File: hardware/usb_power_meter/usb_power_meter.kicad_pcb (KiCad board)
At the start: 4 copper layers, 37 x 39 mm, 39 parts, among them J1 KH-1.27PH180-2X5P-L7.2-SMT, J2 917-P81A202ES60201, J4 A/F LCPTrue color1.2pillar_C4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, Q1 2N7002, Q2 IRML6401, U1 nRF52833-QDxx, U2 INA226, X1 32Mhz crystal, X2 32.768kHz crystal

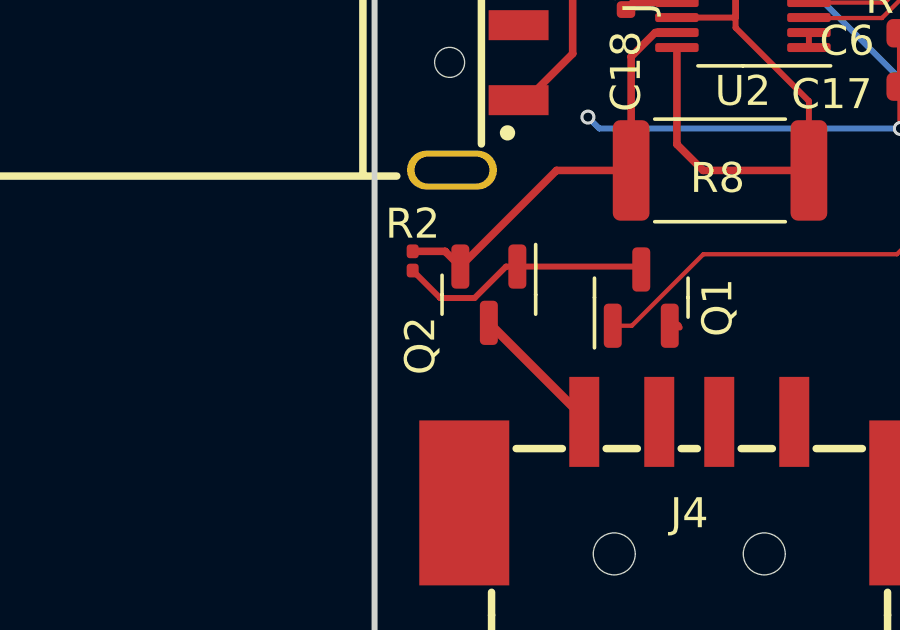
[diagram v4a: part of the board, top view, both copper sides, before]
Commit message: Add a protection diode
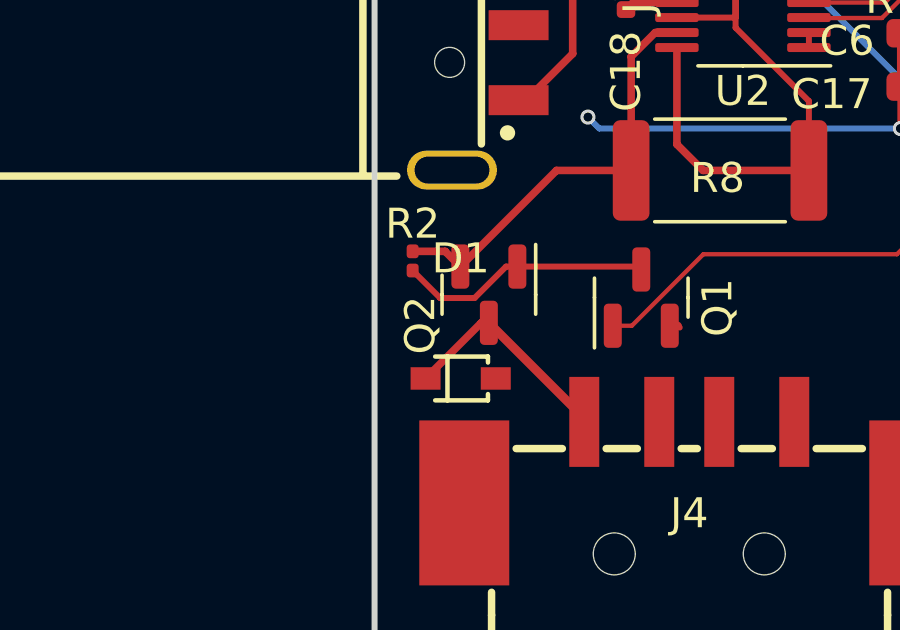
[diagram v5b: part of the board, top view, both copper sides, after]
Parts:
- added D1: 1N5819WS, easyeda2kicad:SOD-323_L1.8-W1.3-LS2.5-RD, F.Cu at (102.9, 83.8)
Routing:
- net Net-(D1-C): track 4.62 -> 7.50 mm
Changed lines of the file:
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@@
   (net 40 "unconnected-(J4-D+-Pad2)")
   (net 41 "unconnected-(J4-D--Pad3)")
-  (net 42 "Net-(J4-VCC)")
+  (net 42 "Net-(D1-C)")
   (net 43 "unconnected-(J4-Pad5)")
   (net 44 "unconnected-(J4-Pad6)")
@@
     (property "ki_keywords" "transistor PMOS P-MOS P-MOSFET")
     (attr smd)
-    (fp_text reference "Q2" (at 1.6995 2.286 90) (layer "F.SilkS")
+    (fp_text reference "Q2" (at 1.0135 2.286 90) (layer "F.SilkS")
         (effects (font (size 1 1) (thickness 0.15)))
     )
@@
       (net 34 "Net-(Q2-S)") (pinfunction "S") (pintype "passive"))
     (pad "3" smd roundrect (at 0.9375 0 270) (size 1.475 0.6) (layers "F.Cu" "F.Paste" "F.Mask") (roundrect_rratio 0.25)
-      (net 42 "Net-(J4-VCC)") (pinfunction "D") (pintype "passive"))
+      (net 42 "Net-(D1-C)") (pinfunction "D") (pintype "passive"))
     (model "${KICAD6_3DMODEL_DIR}/Package_TO_SOT_SMD.3dshapes/SOT-23.wrl"
       (offset (xyz 0 0 0))
@@
       (scale (xyz 1 1 1))
       (rotate (xyz 0 0 0))
+    )
+  )
+  (footprint "easyeda2kicad:SOD-323_L1.8-W1.3-LS2.5-RD" (layer "F.Cu")
+    (at 102.87 83.82)
+    (property "JLC Part" "Basic Part")
+    (property "LCSC Part" "C191023")
+    (property "Manufacturer" "Hottech(合科泰)")
+    (property "Sheetfile" "usb_power_meter.kicad_sch")
+    (property "Sheetname" "")
+    (attr smd)
+    (fp_text reference "D1" (at 0 -4) (layer "F.SilkS")
+        (effects (font (size 1 1) (thickness 0.15)))
+    )
+    (fp_text value "1N5819WS" (at 0 4) (layer "F.Fab")
+        (effects (font (size 1 1) (thickness 0.15)))
+    )
+    (fp_text user "${REFERENCE}" (at 0 0) (layer "F.Fab")
+        (effects (font (size 1 1) (thickness 0.15)))
+    )
+    (fp_line (start -0.85 -0.73) (end 0.91 -0.73)
+      (stroke (width 0.15) (type solid)) (layer "F.SilkS"))
+    (fp_line (start -0.85 0.73) (end 0.91 0.73)
+      (stroke (width 0.15) (type solid)) (layer "F.SilkS"))
+    (fp_line (start -0.44 -0.73) (end -0.44 0.73)
+      (stroke (width 0.15) (type solid)) (layer "F.SilkS"))
+    (fp_line (start 0.91 -0.73) (end 0.91 -0.53)
+      (stroke (width 0.15) (type solid)) (layer "F.SilkS"))
+    (fp_line (start 0.91 0.73) (end 0.91 0.52)
+      (stroke (width 0.15) (type solid)) (layer "F.SilkS"))
+    (fp_circle (center -1.22 0.65) (end -1.19 0.65)
+      (stroke (width 0.06) (type solid)) (fill none) (layer "F.Fab"))
+    (pad "1" smd rect (at -1.17 0) (size 1 0.75) (layers "F.Cu" "F.Paste" "F.Mask")
+      (net 42 "Net-(D1-C)") (pinfunction "C") (pintype "unspecified"))
+    (pad "2" smd rect (at 1.17 0) (size 1 0.75) (layers "F.Cu" "F.Paste" "F.Mask")
+      (net 1 "GND") (pinfunction "A") (pintype "unspecified"))
+    (model "${EASYEDA2KICAD}/easyeda2kicad.3dshapes/SOD-323_L1.7-W1.3-H1.1-LS2.5.wrl"
+      (offset (xyz -0.14 0 -0))
+      (scale (xyz 1 1 1))
+      (rotate (xyz 0 0 180))
     )
   )
@@
       (net 41 "unconnected-(J4-D--Pad3)") (pinfunction "D-") (pintype "unspecified+no_connect"))
     (pad "4" smd rect (at -3.5 -1.35) (size 1 3) (layers "F.Cu" "F.Paste" "F.Mask")
-      (net 42 "Net-(J4-VCC)") (pinfunction "VCC") (pintype "unspecified"))
+      (net 42 "Net-(D1-C)") (pinfunction "VCC") (pintype "unspecified"))
     (pad "5" smd rect (at -7.5 1.35 90) (size 5.5 3) (layers "F.Cu" "F.Paste" "F.Mask")
       (net 43 "unconnected-(J4-Pad5)") (pinfunction "5") (pintype "unspecified+no_connect"))
@@
   (segment (start 106.99 85.268) (end 106.99 85.146) (width 0.3) (layer "F.Cu") (net 42))
   (segment (start 106.99 85.146) (end 103.81 81.966) (width 0.3) (layer "F.Cu") (net 42))
+  (segment (start 101.7 83.82) (end 103.554 81.966) (width 0.254) (layer "F.Cu") (net 42))
+  (segment (start 103.554 81.966) (end 103.81 81.966) (width 0.254) (layer "F.Cu") (net 42))
   (segment (start 125.274 74.22) (end 125.274 73.6555) (width 0.2) (layer "F.Cu") (net 45))
   (segment (start 126.67 87.345) (end 126.67 94.158) (width 0.2) (layer "F.Cu") (net 45))

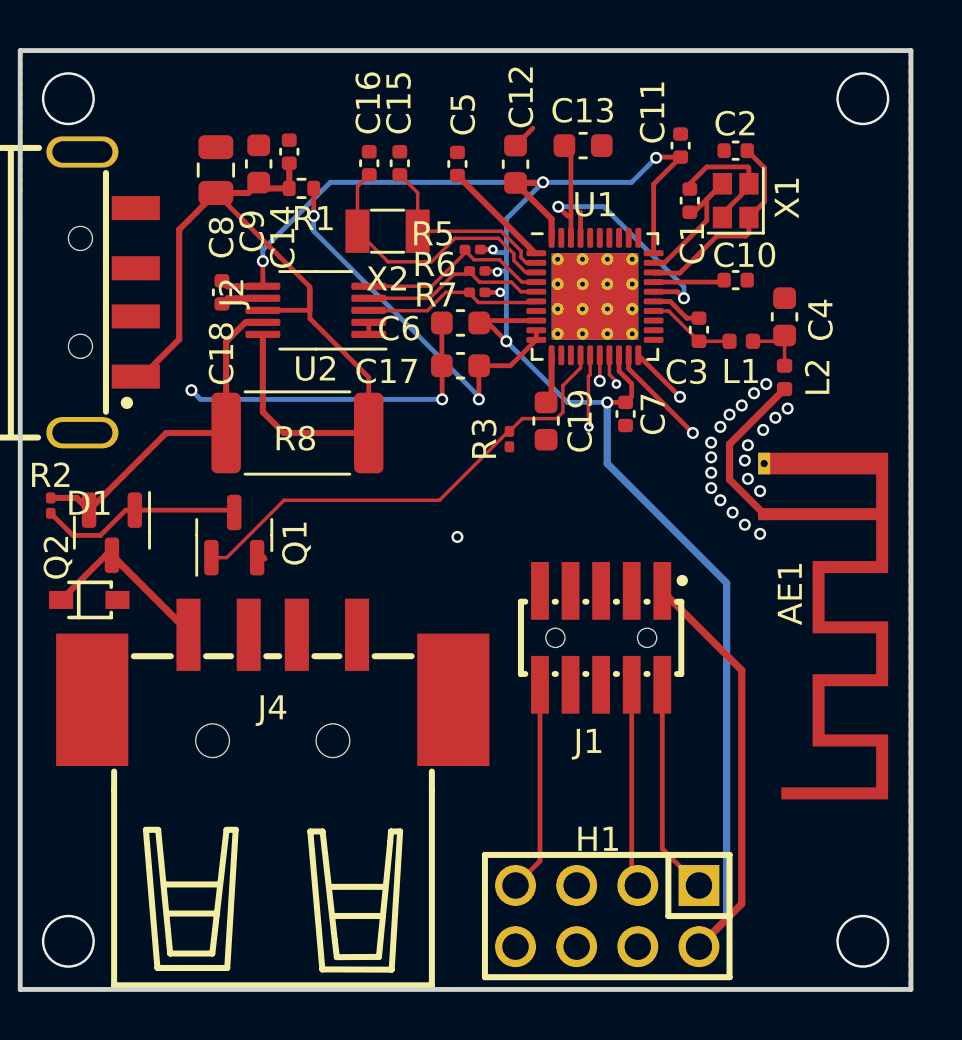
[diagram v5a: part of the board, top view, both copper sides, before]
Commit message: Add stitching vias
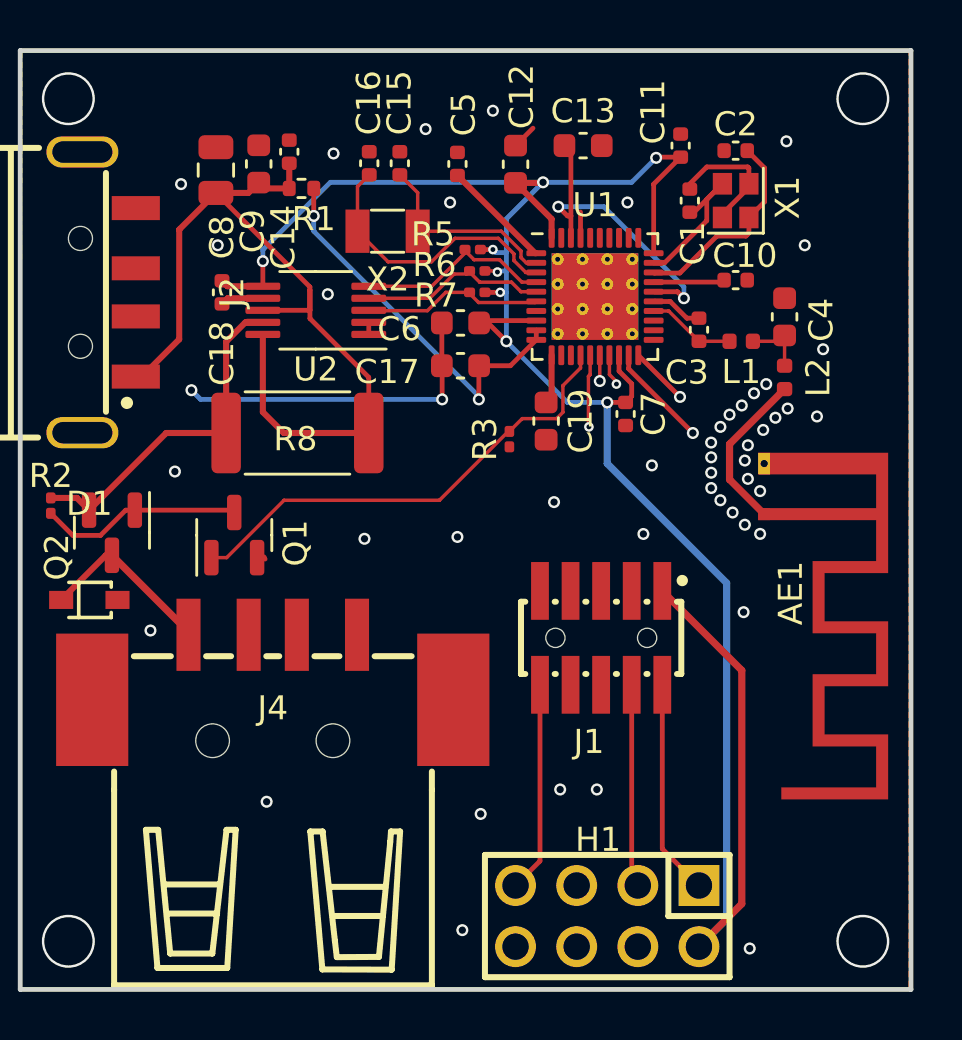
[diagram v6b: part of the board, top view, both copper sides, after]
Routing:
- net GND: vias 26 -> 51
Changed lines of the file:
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@@
   (segment (start 130.218 65.834) (end 128.518 65.834) (width 0.2) (layer "F.Cu") (net 1))
   (segment (start 123.274 68.7805) (end 123.274 67.709) (width 0.2) (layer "F.Cu") (net 1))
+  (via (at 126.238 78.232) (size 0.5) (drill 0.3) (layers "F.Cu" "B.Cu") (free) (net 1))
   (via (at 130.099 80.696) (size 0.5) (drill 0.3) (layers "F.Cu" "B.Cu") (free) (net 1))
   (via (at 118.161 81.204) (size 0.5) (drill 0.3) (layers "F.Cu" "B.Cu") (free) (net 1))
+  (via (at 130.048 84.328) (size 0.5) (drill 0.3) (layers "F.Cu" "B.Cu") (free) (net 1))
+  (via (at 106.426 78.486) (size 0.5) (drill 0.3) (layers "F.Cu" "B.Cu") (free) (net 1))
   (via (at 135 63) (size 2.2) (drill 2) (layers "F.Cu" "B.Cu") (net 1))
+  (via (at 117.856 67.31) (size 0.5) (drill 0.3) (layers "F.Cu" "B.Cu") (free) (net 1))
   (via (at 130.226 77.394) (size 0.5) (drill 0.3) (layers "F.Cu" "B.Cu") (free) (net 1))
   (via (at 130.734 81.077) (size 0.5) (drill 0.3) (layers "F.Cu" "B.Cu") (free) (net 1))
+  (via (at 125.884034 81.080088) (size 0.5) (drill 0.3) (layers "F.Cu" "B.Cu") (free) (net 1))
+  (via (at 119.126 92.71) (size 0.5) (drill 0.3) (layers "F.Cu" "B.Cu") (free) (net 1))
+  (via (at 133.35 73.406) (size 0.5) (drill 0.3) (layers "F.Cu" "B.Cu") (free) (net 1))
   (via (at 130.988 74.854) (size 0.5) (drill 0.3) (layers "F.Cu" "B.Cu") (free) (net 1))
   (via (at 128.698591 77.283465) (size 0.5) (drill 0.3) (layers "F.Cu" "B.Cu") (free) (net 1))
   (via (at 117.526 75.489) (size 0.5) (drill 0.3) (layers "F.Cu" "B.Cu") (free) (net 1))
   (via (at 102 98) (size 2.2) (drill 2) (layers "F.Cu" "B.Cu") (free) (net 1))
+  (via (at 133.096 76.2) (size 0.5) (drill 0.3) (layers "F.Cu" "B.Cu") (free) (net 1))
+  (via (at 114.3 81.28) (size 0.5) (drill 0.3) (layers "F.Cu" "B.Cu") (free) (net 1))
   (via (at 130.226 78.791) (size 0.5) (drill 0.3) (layers "F.Cu" "B.Cu") (free) (net 1))
+  (via (at 130.302 98.298) (size 0.5) (drill 0.3) (layers "F.Cu" "B.Cu") (free) (net 1))
+  (via (at 131.826 64.77) (size 0.5) (drill 0.3) (layers "F.Cu" "B.Cu") (free) (net 1))
   (via (at 128.701465 77.895732) (size 0.5) (drill 0.3) (layers "F.Cu" "B.Cu") (free) (net 1))
+  (via (at 118.364 97.536) (size 0.5) (drill 0.3) (layers "F.Cu" "B.Cu") (free) (net 1))
   (via (at 130.861 76.759) (size 0.5) (drill 0.3) (layers "F.Cu" "B.Cu") (free) (net 1))
   (via (at 128.702 78.537) (size 0.5) (drill 0.3) (layers "F.Cu" "B.Cu") (free) (net 1))
@@
   (via (at 131.369 76.251) (size 0.5) (drill 0.3) (layers "F.Cu" "B.Cu") (free) (net 1))
   (via (at 128.702 79.172) (size 0.5) (drill 0.3) (layers "F.Cu" "B.Cu") (free) (net 1))
+  (via (at 132.588 69.088) (size 0.5) (drill 0.3) (layers "F.Cu" "B.Cu") (free) (net 1))
+  (via (at 123.952 91.694) (size 0.5) (drill 0.3) (layers "F.Cu" "B.Cu") (free) (net 1))
+  (via (at 113.01509 65.275609) (size 0.5) (drill 0.3) (layers "F.Cu" "B.Cu") (free) (net 1))
+  (via (at 116.84 64.262) (size 0.5) (drill 0.3) (layers "F.Cu" "B.Cu") (free) (net 1))
   (via (at 129.464 76.124) (size 0.5) (drill 0.3) (layers "F.Cu" "B.Cu") (free) (net 1))
   (via (at 130.734 79.299) (size 0.5) (drill 0.3) (layers "F.Cu" "B.Cu") (free) (net 1))
+  (via (at 110.236 92.202) (size 0.5) (drill 0.3) (layers "F.Cu" "B.Cu") (free) (net 1))
   (via (at 129.083 76.632) (size 0.5) (drill 0.3) (layers "F.Cu" "B.Cu") (free) (net 1))
+  (via (at 122.428 91.694) (size 0.5) (drill 0.3) (layers "F.Cu" "B.Cu") (free) (net 1))
+  (via (at 106.68 66.548) (size 0.5) (drill 0.3) (layers "F.Cu" "B.Cu") (free) (net 1))
+  (via (at 119.634 63.5) (size 0.5) (drill 0.3) (layers "F.Cu" "B.Cu") (free) (net 1))
+  (via (at 108.204 69.088) (size 0.5) (drill 0.3) (layers "F.Cu" "B.Cu") (free) (net 1))
+  (via (at 125.222 67.31) (size 0.5) (drill 0.3) (layers "F.Cu" "B.Cu") (free) (net 1))
   (via (at 129.591 80.188) (size 0.5) (drill 0.3) (layers "F.Cu" "B.Cu") (free) (net 1))
   (via (at 130.48 75.235) (size 0.5) (drill 0.3) (layers "F.Cu" "B.Cu") (free) (net 1))
+  (via (at 112.776 71.12) (size 0.5) (drill 0.3) (layers "F.Cu" "B.Cu") (free) (net 1))
   (via (at 129.083 79.68) (size 0.5) (drill 0.3) (layers "F.Cu" "B.Cu") (free) (net 1))
   (via (at 107.112 75.108) (size 0.5) (drill 0.3) (layers "F.Cu" "B.Cu") (free) (net 1))
+  (via (at 122.174 79.756) (size 0.5) (drill 0.3) (layers "F.Cu" "B.Cu") (free) (net 1))
   (via (at 131.877 75.87) (size 0.5) (drill 0.3) (layers "F.Cu" "B.Cu") (free) (net 1))
+  (via (at 105.41 85.09) (size 0.5) (drill 0.3) (layers "F.Cu" "B.Cu") (free) (net 1))
   (segment (start 117.526 75.489) (end 107.493 75.489) (width 0.2) (layer "B.Cu") (net 1))
   (segment (start 107.493 75.489) (end 107.112 75.108) (width 0.2) (layer "B.Cu") (net 1))

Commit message: Add switch and LED
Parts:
- added LED1: 0805G (Green), easyeda2kicad:LED0805-R-RD, F.Cu at (113.5, 58.9)
- added R4: 100R Resistor, Resistor_SMD:R_0603_1608Metric, F.Cu at (112.3, 61.9)
- added SW1: TS-1187A-B-A-B, easyeda2kicad:SW-SMD_4P-L5.1-W5.1-P3.70-LS6.5-TL-2, F.Cu at (126.5, 59.9)
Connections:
- U1 pad 35: unconnected-(U1-AIN6/P0.30-Pad35) -> Net-(SW1-A)
- U1 pad 36: unconnected-(U1-AIN7/P0.31-Pad36) -> Net-(LED1-K)
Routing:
- net Net-(LED1-K): track 0.00 -> 15.0 mm, vias 0 -> 2
- net Net-(SW1-A): track 0.00 -> 9.88 mm, vias 0 -> 2
- net VDD: track 95.1 -> 100.8 mm, vias 8 -> 9
- net GND: track 27.3 -> 30.5 mm, vias 51 -> 50
- net Net-(LED1-A): track 0.00 -> 2.25 mm
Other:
- board size 37 x 39 mm -> 37 x 44 mm

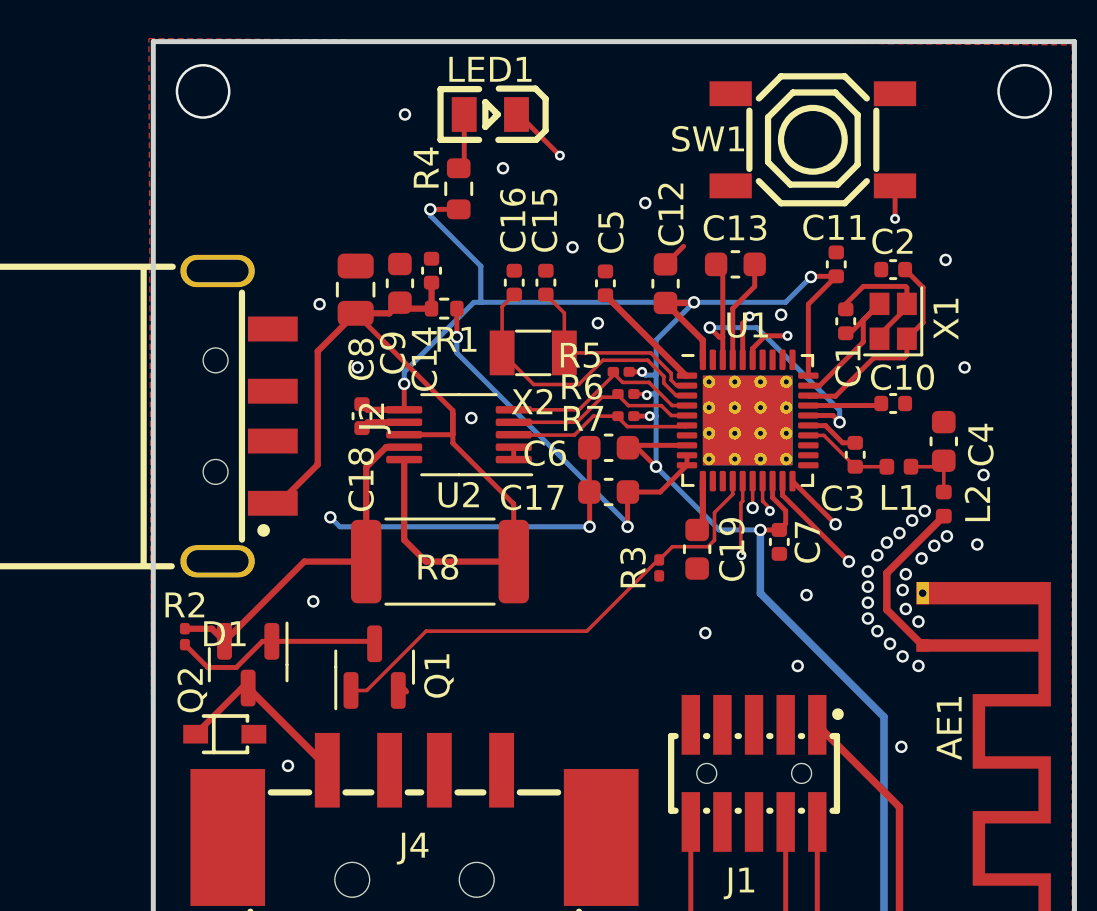
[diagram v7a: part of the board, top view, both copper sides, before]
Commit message: Fix via sizes and 10k resistor footprint
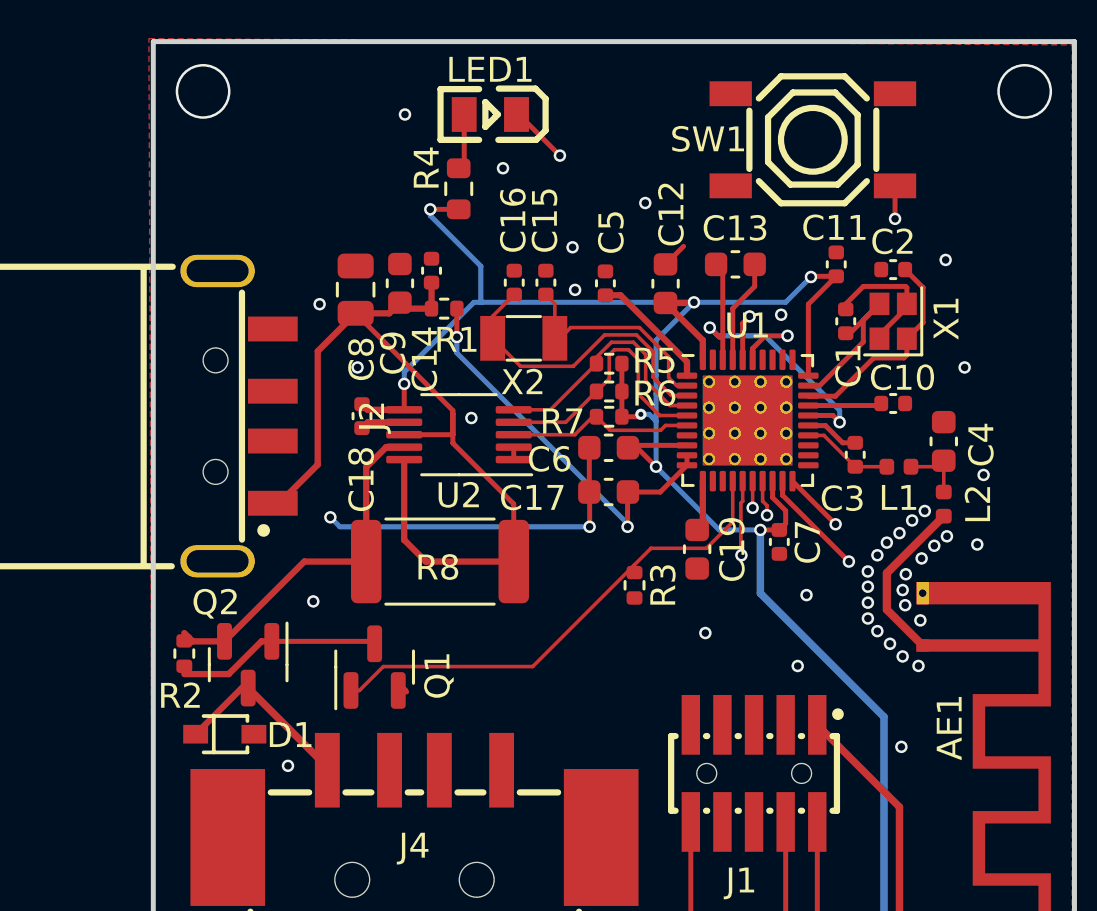
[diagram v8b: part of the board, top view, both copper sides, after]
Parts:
- R2, R3, R5, R6, R7: footprint Resistor_SMD:R_0201_0603Metric -> Resistor_SMD:R_0402_1005Metric
- moved R3 1.21 mm to (119.3, 77.8)
- moved X2 0.70 mm to (114.9, 67.9)
- moved R6 0.68 mm to (118.3, 70.1)
- moved R2 0.68 mm to (101.2, 80.6)
- moved R7 0.67 mm to (118.3, 71.1)
- moved R5 0.59 mm to (118.3, 68.9)
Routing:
- net Net-(U1-AIN3/P0.05): track 7.81 -> 10.6 mm
- net Net-(U1-AIN2/P0.04): track 8.26 -> 9.91 mm
- net Net-(U1-XL2/P0.01): track 11.6 -> 12.5 mm
- net VDD: track 100.8 -> 101.5 mm, vias 9 -> 7
- net Net-(U1-XL1/P0.00): track 8.28 -> 8.85 mm
